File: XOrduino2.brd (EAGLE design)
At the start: 81.3 x 53.3 mm, 83 parts, among them J1 10x1F-H8.5, J2 8x1F-H8.5, J3 8x1F-H8.5, J4 6x1F-H8.5, J5 2.5mm, J6 2.5mm, J7 2.5mm, J8 2.5mm, P1 10k, Q1 TEMT6000, SW3 LEFT BUMPER, SW4 RIGHT BUMPER, U1 ATMEGA32U4-XUAU, U2 LMV358, U3 NJU7261, U4 DRV8833PWP, U5 QRE1113GR, U6 QRE1113GR, X1 USBPCB, X2 USBMINIB, Y1 16MHz

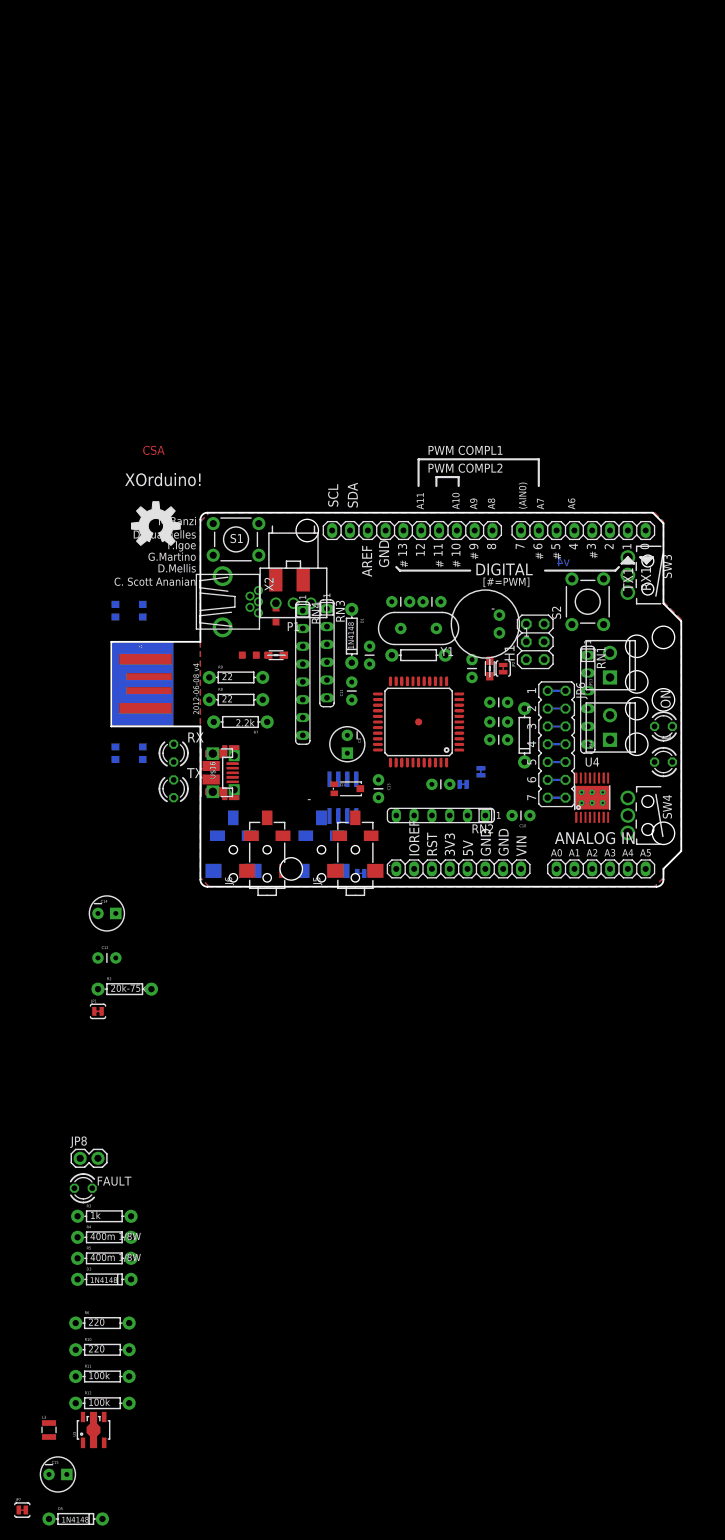
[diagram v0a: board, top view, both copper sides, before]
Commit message: First version of Xorduino2 (v5) board w/ all components placed.
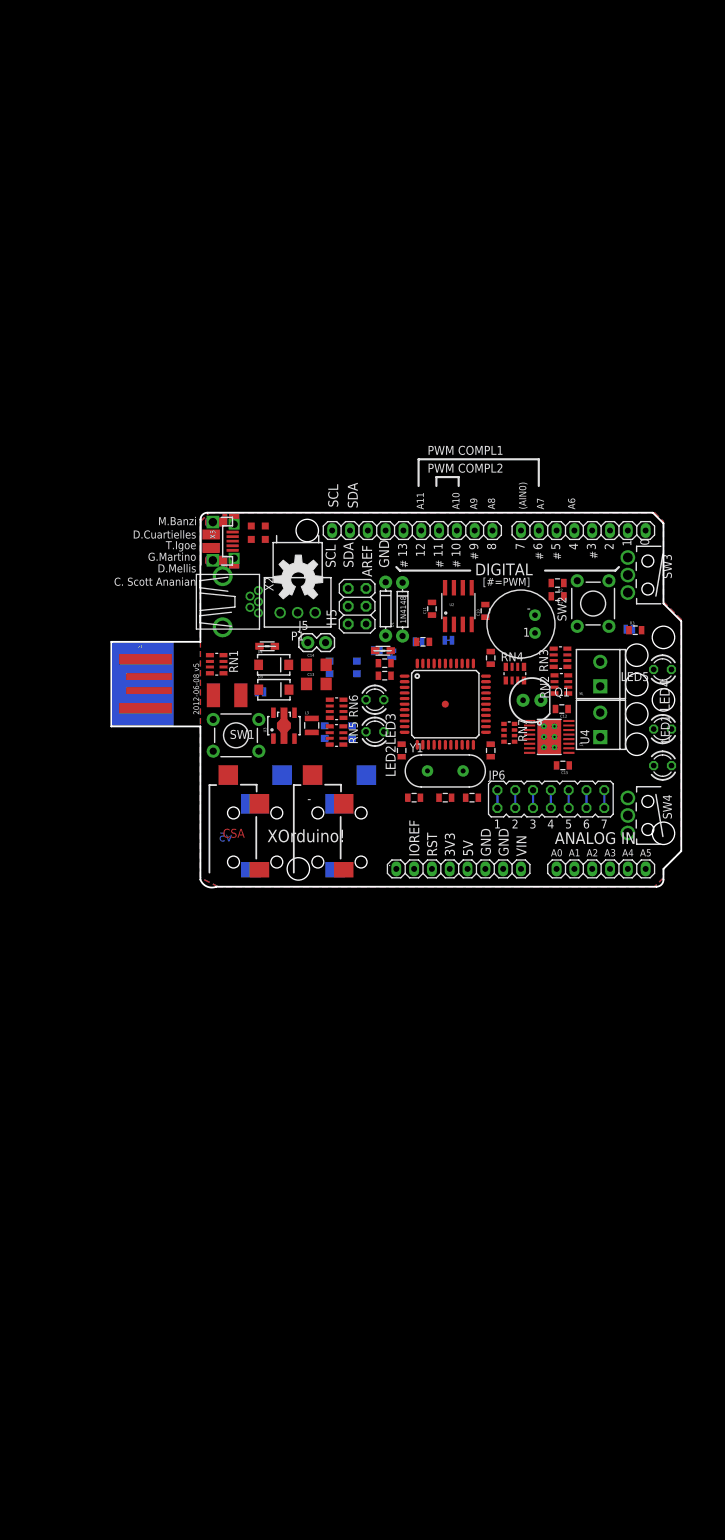
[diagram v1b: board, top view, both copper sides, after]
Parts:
- removed D5: 1N4148, SparkFun-DiscreteSemi:DIODE-1N4148
- removed FAULT, RX, TX: Red, led:LED3MM
- removed J8: 2.5mm, SparkFun:STEREOJACK2.5MM_SMD
- removed JP13: MOT L, SparkFun:SCREWTERMINAL-3.5MM-2
- removed JP14: MOT R, SparkFun:SCREWTERMINAL-3.5MM-2
- removed JP8: (no value), SparkFun-Connectors:1X02
- removed L: Yellow, led:LED3MM
- removed ON: Green, led:LED3MM
- removed R10, R6: 220, SparkFun-Passives:AXIAL-0.3
- removed R11, R12: 100k, SparkFun-Passives:AXIAL-0.3
- removed R4, R5: 400m 1/8W, SparkFun-Passives:AXIAL-0.3
- removed R7: 2.2k, SparkFun-Passives:AXIAL-0.3
- removed R8, R9: 22, SparkFun-Passives:AXIAL-0.3
- removed S1: RESET, SparkFun-Electromechanical:TACTILE-PTH
- removed S2: 6mm Button, SparkFun-Electromechanical:TACTILE-PTH
- removed U$16: USBMICROB, xorduino:USB-MICROB
- added D4: 1A Schottkey, SparkFun-DiscreteSemi:SMA-DIODE
- added H2, H3: 8x1F-H8.5, SmartPrj:1X08
- added H4: 6x1F-H8.5, SmartPrj:1X06
- added H5: ICSP, SmartPrj:2X03
- added LED1: L Yellow, led:LED3MM
- added LED2: TX Red, led:LED3MM
- added LED3: RX Red, led:LED3MM
- added LED4: ON Green, led:LED3MM
- added LED5: FAULT Red, led:LED3MM
- added RN5: 100k, xorduino:CRA06S
- added RN6: 220, xorduino:CRA06S
- added RN7: 1ohm 1/16W, resistor-dil:EXB38V
- added SW1: RESET, SparkFun-Electromechanical:TACTILE-PTH
- added SW2: 6mm Button, SparkFun-Electromechanical:TACTILE-PTH
- added X3: USBMICROB, xorduino:USB-MICROB
- C1, C2: value 100n -> 18p; device SparkFun-Passives:CAP-PTH-SMALL -> SparkFun-Passives:0805
- C10: value 0.1uF -> 0.22uF; device SparkFun-Passives:CAP-PTH-SMALL -> SparkFun-Passives:0805
- C11: value 0.22uF -> 0.33uF; device SparkFun-Passives:CAP-PTH-SMALL -> SparkFun-Passives:0805
- C12: value 0.01uF -> 10uF; device SparkFun-Passives:CAP-PTH-SMALL -> SparkFun-Passives:0805
- C13: value 0.33uF -> 22uF; device SparkFun-Passives:CAP-PTH-SMALL -> SparkFun-Passives:1206
- C14: value 10uF -> 22uF; device SparkFun-Passives:CPOL-RADIAL-10UF-25V -> SparkFun-Passives:1206
- C15: value 22uF -> 0.01uF; device SparkFun-Passives:CPOL-RADIAL-10UF-25V -> SparkFun-Passives:0805
- C3, C4: value 18p -> 100n; device SparkFun-Passives:CAP-PTH-SMALL -> SparkFun-Passives:0805
- C5, C7: value 1uF -> 100n; device SparkFun-Passives:CAP-PTH-SMALL -> SparkFun-Passives:0805
- C6: device SparkFun-Passives:CAP-PTH-SMALL -> SparkFun-Passives:0805
- C8: value 22uF -> 1uF; device SparkFun-Passives:CPOL-RADIAL-10UF-25V -> SparkFun-Passives:0805
- C9: value 100n -> 1uF; device SparkFun-Passives:CAP-PTH-SMALL -> SparkFun-Passives:0805
- D3: value 1N4148 -> 1A Schottkey; device SparkFun-DiscreteSemi:DIODE-1N4148 -> SparkFun-DiscreteSemi:SMA-DIODE
- F1: value MF-MSMF050-2 500mA -> 0ZCC0110FF2C 1.1A
- H1: value ICSP -> 10x1F-H8.5; device SmartPrj:2X03 -> SmartPrj:1X10
- J1: value 10x1F-H8.5 -> 2.5mm; device SmartPrj:1X10 -> xorduino:MJ-3523-SMT
- J2, J3: value 8x1F-H8.5 -> 2.5mm; device SmartPrj:1X08 -> xorduino:MJ-3523-SMT
- J4: value 6x1F-H8.5 -> 2.5mm; device SmartPrj:1X06 -> xorduino:MJ-3523-SMT
- J5: value 2.5mm -> Batt In; device SparkFun:STEREOJACK2.5MM_SMD -> SparkFun-Connectors:1X02
- J6: value 2.5mm -> MOT L; device SparkFun:STEREOJACK2.5MM_SMD -> SparkFun:SCREWTERMINAL-3.5MM-2
- J7: value 2.5mm -> MOT R; device SparkFun:STEREOJACK2.5MM_SMD -> SparkFun:SCREWTERMINAL-3.5MM-2
- Q1: value TEMT6000 -> ALS-PT204-6C/L177; device SparkFun:TEMT6000-SEN -> xorduino:LED3MM-KIT
- R1, R3: device SparkFun-Passives:AXIAL-0.3 -> SparkFun-Passives:0805
- R2: value 20k-75k -> 2.2k; device SparkFun-Passives:AXIAL-0.3 -> SparkFun-Passives:0805
- RN1: value 10k -> 22; device resistor-sil:SIL6 -> xorduino:CRA06S
- RN2: device resistor-sil:SIL6 -> xorduino:CRA06S
- RN3: value 100k -> 1k; device resistor-sil:SIL6 -> xorduino:CRA06S
- RN4: value 1k -> 100k; device resistor-sil:SIL8 -> xorduino:CRA06S
- moved C15 124.1 mm to (64.4, 17.3), turned to 180 degrees
- moved JP7 121.5 mm to (21.3, 27.8), flipped to the bottom
- moved R3 112.8 mm to (74.7, 36.6)
- moved L3 107.2 mm to (28.6, 23.0)
- moved U3 104.0 mm to (24.6, 23.0)
- moved JP1 93.3 mm to (73.9, 36.7), flipped to the bottom, turned to 180 degrees
- moved D3 87.5 mm to (23.2, 28.1)
- moved R2 84.6 mm to (63.6, 43.3), turned to 180 degrees
- moved C12 75.1 mm to (64.2, 25.3), turned to 180 degrees
- moved J2 67.0 mm to (23.6, 0.02), flipped to the bottom, turned to 90 degrees
- moved J1 56.8 mm to (17.4, 0.02), turned to 90 degrees
- moved J6 54.8 mm to (69.7, 28.6)
- moved RN1 53.2 mm to (15.0, 31.7)
- moved C14 46.4 mm to (29.2, 31.6)
- moved J7 44.5 mm to (69.7, 21.3), flipped to the top
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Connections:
- removed net N$21: R5.P$2, U4.3
- new net N$20: RN7.1, RN7.2, U4.3
- net +3V3: now also H3.4; no longer J3.4
- net +5V: now also C11.1, C3.2, C4.1, C5.1, H3.2, H3.5, H5.2, RN2.5, RN2.8, RN3.5, RN3.7, RN5.7, RN5.8; no longer C1.1, C2.1, C8.1, C9.2, H1.2, J3.2, J3.5, R11.P$1, R12.P$1, RN1.1, RN2.2, RN4.2, RN4.4
- net A0: now also H4.1; no longer J4.1
- net A1: now also H4.2; no longer J4.2
- net A2: now also H4.3; no longer J4.3
- net A3: now also H4.4; no longer J4.4
- net A4: now also H4.5; no longer J4.5
- net A5: now also H4.6; no longer J4.6
- net AREF: now also H1.8; no longer J1.8
- net AVCC: now also C8.1; no longer C5.1
- net D+: now also RN1.1, X3.D+; no longer R9.P$1, U$16.D+
- net D-: now also RN1.2, X3.D-; no longer R8.P$1, U$16.D-
- net D0/RX: now also H2.1; no longer J2.1
- net D1/TX: now also H2.2; no longer J2.2
- net D2/SDA: now also H1.9, H2.3; no longer J1.9, J2.3
- net D3/SCL: now also H1.10, H2.4; no longer J1.10, J2.4
- net D4: now also H2.5; no longer J2.5
- net D5*: now also H2.6; no longer J2.6
- net D6*: now also H2.7; no longer J2.7
- net D7: now also H2.8; no longer J2.8
- net GND: now also C1.1, C10.1, C12.2, C13.2, H1.7, H3.6, H3.7, H5.6, J1.1, J2.1, J3.1, J4.1, J5.2, LED1.K, LED4.K, Q1.A, R2.1, RN2.3, RN2.7, RN4.7, RN7.5, RN7.6, RN7.7, RN7.8, SW1.4, SW2.4; no longer C1.2, C11.1, C15.2, C9.1, H1.6, J1.7, J3.6, J3.7, J5.1, J5.5, J6.1, J6.5, J7.1, J7.5, J8.1, J8.5, JP8.2, L.K, ON.K, Q1.EMITTER, R4.P$1, R5.P$1, R7.P$1, RN2.4, RN2.5, RN3.3, S1.4, S2.4
- net HWB: now also RN2.2; no longer RN2.3
- net IO10*: now also H1.3; no longer J1.3
- net IO11*: now also H1.4; no longer J1.4
- net IO12: now also H1.5, SW2.1; no longer J1.5, S2.1
- net IO13*: now also H1.6; no longer J1.6
- net IO8: now also H1.1, RN5.1; no longer J1.1, R11.P$2
- net IO9*: now also H1.2, RN5.2; no longer J1.2, R12.P$2
- net LIGHT: now also C11.2, Q1.K, RN4.1; no longer C13.2, Q1.COLLECTOR, RN3.5
- net MISO: now also H5.1; no longer H1.1
- net MOSI: now also H5.4; no longer H1.4
- net MOTL+: now also J6.1; no longer JP13.1
- net MOTL-: now also J6.2; no longer JP13.2
- net MOTR+: now also J7.2; no longer JP14.2
- net MOTR-: now also J7.1; no longer JP14.1
- net N$1: now also LED3.A, RN3.3; no longer RN4.3, TX.A
- net N$10: now also C12.1; no longer C14.1
- net N$11: now also C7.2; no longer C10.2
- net N$12: now also LED5.K; no longer FAULT.K
- net N$13: now also RN6.7; no longer R10.P$1
- net N$15: now also RN6.8; no longer R6.P$1
- net N$16: now also RN4.3; no longer RN3.1
- net N$17: now also D4.A, J5.1; no longer D3.A, JP8.1
- net N$18: now also LED5.A, R3.2; no longer FAULT.A, R3.P$2
- net N$19: now also RN7.3, RN7.4; no longer R4.P$2
- net N$2: now also LED1.A, RN3.1; no longer L.A, RN4.5
- net N$3: now also LED4.A, RN3.4; no longer ON.A, RN4.7
- net N$4: now also LED2.A, RN3.2; no longer RN4.1, RX.A
- net N$5: now also R2.2, RN4.6; no longer R7.P$2, RN3.2
- net N$6: now also RN3.8; no longer RN4.6
- net N$7: now also C15.1; no longer C12.1
- net N$8: now also RN5.5, RN5.6; no longer R2.P$1
- net N$9: now also C7.1, RN2.4; no longer C10.1, RN1.2
- net RA: now also J1.2; no longer J5.4, RN1.3
- net RB: now also J2.2; no longer J6.4, RN1.4
- net RC: now also J3.2; no longer J7.4, RN1.5
- net RD: now also J4.2; no longer J8.4, RN1.6
- net RD+: now also RN1.8; no longer R9.P$2
- net RD-: now also RN1.7; no longer R8.P$2
- net RESET: now also H3.3, H5.5, SW1.1; no longer H1.5, J3.3, S1.1
- net RXLED: now also LED3.K; no longer RX.K
- net SCK: now also H5.3; no longer H1.3
- net SOUND: now also C10.2, RN4.2; no longer C11.2, RN3.4
- net TXLED: now also LED2.K; no longer TX.K
- net UCAP: now also C9.1; no longer C7.1
- net UGND: now also C9.2, X3.GND; no longer C7.2, U$16.GND
- net VIN: now also C14.1, C15.2, D4.C, H3.8, R3.1, RN5.3, RN5.4, RN6.1, RN6.2; no longer C12.2, C15.1, D5.C, J3.8, R10.P$2, R2.P$2, R3.P$1, R6.P$2
- net VUSB: now also D3.A; no longer D5.A
- net XTAL1: now also C2.1, R1.1; no longer C4.1, R1.P$1
- net XTAL2: now also C1.2, R1.2; no longer C3.2, R1.P$2
- net XUSB: now also X3.VBUS; no longer U$16.VBUS
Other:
- board size 81.3 x 53.3 mm -> 81.3 x 53.5 mm
- board text added: "2012-06-08 v5"
- board text added: "v5"
- board text removed: "2012-06-08 v4"
- board text removed: "v4"

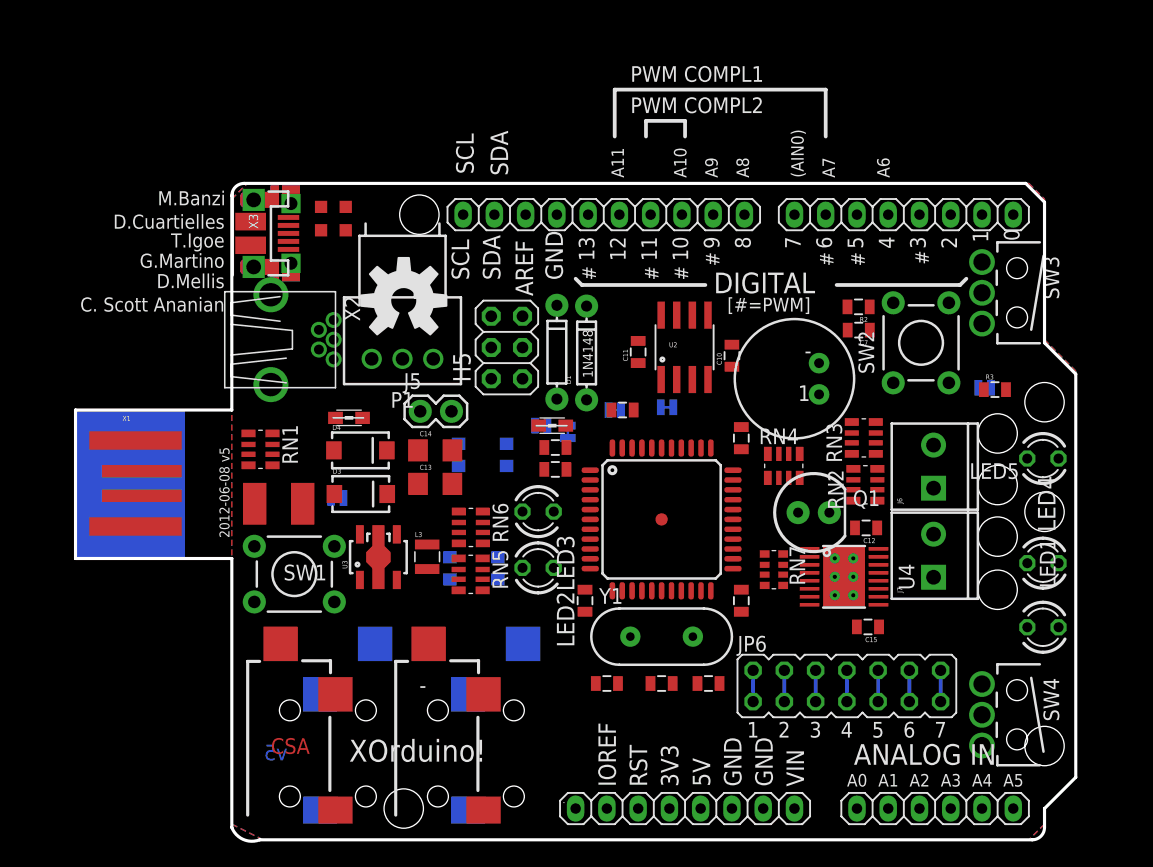
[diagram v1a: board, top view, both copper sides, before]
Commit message: 70% 2-layer routed version of XOrduino2.
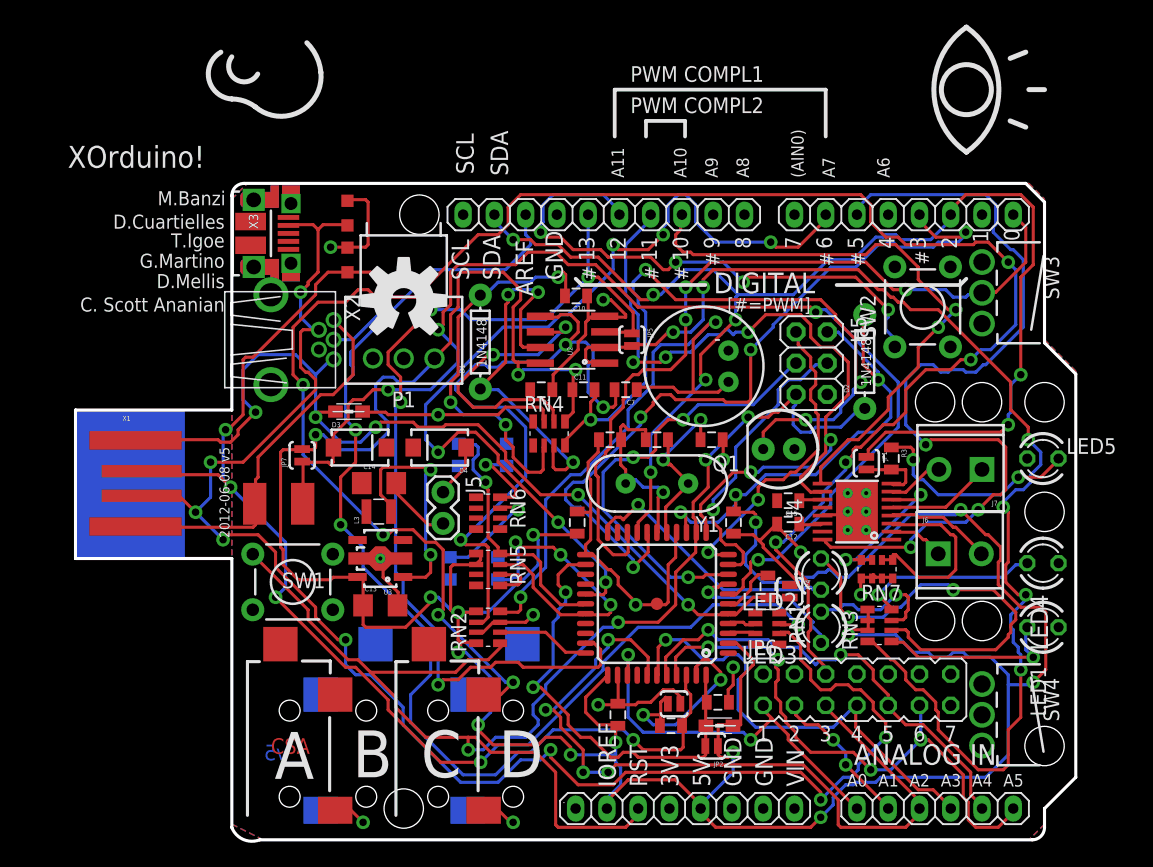
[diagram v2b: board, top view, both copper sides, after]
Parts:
- J6: value MOT L -> MOT R
- J7: value MOT R -> MOT L
- JP1, JP2, JP3, JP4, JP5, JP7: device SparkFun-Passives:SJ_2S-TRACE -> xorduino:SJ-2S-TRACE-NOCONFLICT
- JP6: device xorduino:JP7QS -> xorduino:JP7QS-NOCONFLICT
- SW3: device xorduino:SW-LEVER-V1 -> xorduino:SW-LEVER-V1-NOHOLES
- SW4: device xorduino:SW-LEVEL-V2 -> xorduino:SW-LEVER-V2-NOHOLES
- moved RN1 43.7 mm to (56.2, 17.2)
- moved RN2 32.8 mm to (33.5, 17.3)
- moved JP2 29.5 mm to (51.7, 7.62), flipped to the top
- moved L1 27.9 mm to (52.3, 9.27), turned to 180 degrees
- moved R2 26.6 mm to (37.8, 36.6)
- moved C6 26.0 mm to (48.4, 9.27)
- moved D2 25.0 mm to (64.1, 38.9)
- moved LED3 24.8 mm to (60.6, 17.3), turned to 270 degrees
- moved H5 24.8 mm to (59.8, 38.7)
- moved C3 24.6 mm to (44.1, 10.2), turned to 270 degrees
- moved C8 24.6 mm to (52.2, 11.2), turned to 0 degrees
- moved JP3 24.4 mm to (48.6, 11.0), flipped to the top, turned to 0 degrees
- moved LED2 23.0 mm to (60.6, 21.6), turned to 270 degrees
- moved JP4 22.2 mm to (58.0, 20.2), flipped to the top
- moved C1 21.6 mm to (51.7, 32.5), turned to 180 degrees
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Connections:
- net +5V: now also P1.1, RN4.5, RN5.1, RN5.2; no longer P1.3, RN4.8, RN5.7, RN5.8
- net D+: now also RN1.7; no longer RN1.1
- net D-: now also RN1.6; no longer RN1.2
- net GND: now also P1.3, U3.VIA1; no longer P1.1
- net IO8: now also RN5.8; no longer RN5.1
- net IO9*: now also RN5.7; no longer RN5.2
- net LIGHT: now also RN4.4; no longer RN4.1
- net MOTL+: now also J7.2, U4.7; no longer J6.1, U4.2
- net MOTL-: now also J7.1, U4.5; no longer J6.2, U4.4
- net MOTR+: now also J6.1, U4.2; no longer J7.2, U4.7
- net MOTR-: now also J6.2, U4.4; no longer J7.1, U4.5
- net N$12: now also R3.2; no longer LED5.K
- net N$18: now also LED5.K, R3.1; no longer LED5.A, R3.2
- net RD+: now also RN1.2; no longer RN1.8
- net RD-: now also RN1.3; no longer RN1.7
- net VIN: now also LED5.A; no longer R3.1
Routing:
- net +5V: track 0.00 -> 319.4 mm, vias 0 -> 19
- net RC: track 0.00 -> 156.3 mm, vias 0 -> 8
- net D-: track 0.00 -> 132.4 mm, vias 0 -> 8
- net GND: track 0.00 -> 123.8 mm, vias 0 -> 12
- net RESET: track 0.00 -> 113.9 mm, vias 0 -> 4
- net D+: track 0.00 -> 109.8 mm, vias 0 -> 6
- net D2/SDA: track 0.00 -> 107.9 mm, vias 0 -> 7
- net N$6: track 0.00 -> 99.1 mm, vias 0 -> 6
- net VUSB: track 0.00 -> 96.1 mm, vias 0 -> 4
- net AREF: track 0.00 -> 88.4 mm, vias 0 -> 3
- net IO13*: track 0.00 -> 79.8 mm, vias 0 -> 4
- net UGND: track 0.00 -> 77.1 mm, vias 0 -> 5
- net D6*: track 0.00 -> 73.4 mm, vias 0 -> 6
- net D5*: track 0.00 -> 69.7 mm, vias 0 -> 3
- net D0/RX: track 0.00 -> 65.0 mm, vias 0 -> 3
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- added copper zone on layer 1, net VIN
- removed copper zone on layer 1, net +5V
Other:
- board text added: "A"
- board text added: "B"
- board text added: "C"
- board text added: "D"
- board text removed: "-"
